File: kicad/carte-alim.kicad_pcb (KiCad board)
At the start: 2 copper layers, 96.5 x 45.7 mm, 52 parts, among them P1 BATT, P10 5V, P11 5V, P12 5V, P13 5V, P14 5V, P15 5V, P16 5V, P17 3.3V, P18 3.3V, P19 3.3V, P2 BATT, P20 3.3V, P21 3.3V, P22 3.3V, P23 3.3V, P24 3.3V, P25 3.3V, P26 3.3V, P27 MASSE, P28 MASSE, P29 PILES, P3 BATT, P30 CONN_1, P31 CONN_1, P32 CONN_1, P4 BATT, P5 BATT, P6 BATT, P7 5V, P8 5V, P9 5V, U1 LM_1117_3.3, U2 OKI_78SR_5

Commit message: Mise en qualité du typon
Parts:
- removed P1: BATT, KK_2C
- removed P21, P26: 3.3V, KK_2C
- added P33: CONN_1, Mounting_Holes:MountingHole_3.2mm_M3_Pad, F.Cu at (208.9, 66.7)
- C1, C2, C3, C4: footprint C2 -> Capacitors_THT:C_Rect_L7.0mm_W3.5mm_P2.50mm_P5.00mm
- C5, C6, C7, C8: footprint C2V10 -> Capacitors_THT:CP_Radial_D10.0mm_P2.50mm_P5.00mm
- D1, D2, D3, D4: footprint D4 -> Diodes_THT:D_DO-15_P10.16mm_Horizontal
- D5, D6, D7: footprint LED-3MM -> LEDs:LED_D3.0mm
- P10, P11, P12, P13, P14, P15, P16, P17, P18, P19, P2, P20, P22, P23, P24, P25, P29, P3, P4, P5, P6, P7, P8, P9: footprint KK_2C -> EPSA_Connect:KK_2C
- P27, P28: footprint SIL-8 -> Pin_Headers:Pin_Header_Straight_1x08_Pitch2.54mm
- P30, P31, P32: footprint 1pin -> Mounting_Holes:MountingHole_3.2mm_M3_Pad
- R1, R2, R3: footprint R3 -> Resistors_THT:R_Axial_DIN0207_L6.3mm_D2.5mm_P7.62mm_Horizontal
- U1: value LM_1117_3.3 -> LM 1117 3.3; footprint TO220_VERTICAL -> TO_SOT_Packages_THT:TO-220-3_Vertical
- U2: value OKI_78SR_5 -> OKI 78SR 5; footprint TO220_VERTICAL -> TO_SOT_Packages_THT:TO-220-3_Vertical
- moved P31 31.7 mm to (121.3, 103.5)
- moved P27 12.9 mm to (205.1, 94.6), turned to 180 degrees
- moved P28 12.7 mm to (209.6, 94.6), turned to 180 degrees
- moved P30 8.47 mm to (121.3, 66.7)
- moved P32 8.28 mm to (208.9, 103.5)
- moved P29 5.72 mm to (128.9, 102.9)
- moved D1 5.08 mm to (120.7, 83.8), turned to 270 degrees
- moved D2 5.08 mm to (128.3, 83.8), turned to 270 degrees
- moved D3 5.08 mm to (124.5, 94.0), turned to 90 degrees
- moved D4 5.08 mm to (132.1, 94.0), turned to 90 degrees
- moved R1 3.81 mm to (171.4, 96.5)
- moved R2 3.81 mm to (191.8, 96.5)
- moved R3 3.81 mm to (143.5, 92.7)
- moved U1 2.54 mm to (180.3, 78.7), turned to 270 degrees
- moved U2 2.54 mm to (148.6, 78.7), turned to 270 degrees
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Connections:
- net +3.3V renamed +3V3
- D1 pad 1: N-000009 -> +BATT
- D1 pad 2: +BATT -> Net-(D1-Pad2)
- D2 pad 1: N-000005 -> +BATT
- D2 pad 2: +BATT -> Net-(D2-Pad2)
- D3 pad 1: GND -> Net-(D1-Pad2)
- D3 pad 2: N-000009 -> GND
- D4 pad 1: GND -> Net-(D2-Pad2)
- D4 pad 2: N-000005 -> GND
- P29 pad 1: N-000009 -> Net-(D1-Pad2)
- P29 pad 2: N-000005 -> Net-(D2-Pad2)
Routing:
- net GND: track 0.00 -> 47.7 mm
- net +3V3: track 123.6 -> 104.5 mm
- net N-000005: track 14.3 -> 0.00 mm
- net Net-(D1-Pad2): track 0.00 -> 14.0 mm
- net Net-(D2-Pad2): track 0.00 -> 12.7 mm
- net N-000009: track 12.5 -> 0.00 mm
- net +5V: track 129.8 -> 132.9 mm
- net +BATT: track 151.6 -> 148.6 mm
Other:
- outline, holes or cut-outs redrawn
- net class GND added: clearance 0.254, trace_width 0.5, via_dia 1.6002, via_drill 0.8001
- board text added: "Carte alimentation ERACL 2018"
- board text removed: "Carte alimentation 2017-2018"

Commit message: Réalisation du typon avec connecteurs Mini-Fit
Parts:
- removed the C1 at (137.2, 87.6)
- removed the C5 at (139.7, 80.0)
- removed D4: 5A, Diodes_THT:D_DO-15_P10.16mm_Horizontal
- removed D5, D6, D7: GREEN, LEDs:LED_D3.0mm
- removed P10, P11, P12, P13, P14, P15, P16, P9: 5V, EPSA_Connect:KK_2C
- removed P17, P18, P19, P20, P22, P23, P24, P25: 3.3V, EPSA_Connect:KK_2C
- removed the P2 at (137.2, 102.9)
- removed P28: MASSE, Pin_Headers:Pin_Header_Straight_1x08_Pitch2.54mm
- removed P29: PILES, EPSA_Connect:KK_2C
- removed the P3 at (143.5, 102.9)
- removed the P5 at (137.2, 67.3)
- removed the P6 at (143.5, 67.3)
- added J1: PWR_OUT, Connectors_Molex:Molex_MiniFit-JR-5569-04A2_2x02x4.20mm_Angled, F.Cu at (159.4, 94.0)
- added J10: PWR_OUT, Connectors_Molex:Molex_MiniFit-JR-5569-04A2_2x02x4.20mm_Angled, F.Cu at (154.9, 76.2)
- added J2: PWR_OUT, Connectors_Molex:Molex_MiniFit-JR-5569-04A2_2x02x4.20mm_Angled, F.Cu at (169.5, 94.0)
- added J3: PWR_OUT, Connectors_Molex:Molex_MiniFit-JR-5569-04A2_2x02x4.20mm_Angled, F.Cu at (179.7, 94.0)
- added J4: PWR_OUT, Connectors_Molex:Molex_MiniFit-JR-5569-04A2_2x02x4.20mm_Angled, F.Cu at (189.9, 94.0)
- added J5: PWR_OUT, Connectors_Molex:Molex_MiniFit-JR-5569-04A2_2x02x4.20mm_Angled, F.Cu at (200.0, 94.0)
- added J6: PWR_OUT, Connectors_Molex:Molex_MiniFit-JR-5569-04A2_2x02x4.20mm_Angled, F.Cu at (195.6, 76.2)
- added J7: PWR_OUT, Connectors_Molex:Molex_MiniFit-JR-5569-04A2_2x02x4.20mm_Angled, F.Cu at (185.4, 76.2)
- added J8: PWR_OUT, Connectors_Molex:Molex_MiniFit-JR-5569-04A2_2x02x4.20mm_Angled, F.Cu at (175.3, 76.2)
- added J9: PWR_OUT, Connectors_Molex:Molex_MiniFit-JR-5569-04A2_2x02x4.20mm_Angled, F.Cu at (165.1, 76.2)
- D1: value 5A -> YELLOW; footprint Diodes_THT:D_DO-15_P10.16mm_Horizontal -> LEDs:LED_D3.0mm
- D2: value 5A -> RED; footprint Diodes_THT:D_DO-15_P10.16mm_Horizontal -> LEDs:LED_D3.0mm
- D3: value 5A -> ORANGE; footprint Diodes_THT:D_DO-15_P10.16mm_Horizontal -> LEDs:LED_D3.0mm
- P1: renamed from P33; value CONN_1 -> MECA
- P2: renamed from P30; value CONN_1 -> MECA
- P3: renamed from P31; value CONN_1 -> MECA
- P4: value BATT -> PILES; footprint EPSA_Connect:KK_2C -> Connectors_Molex:Molex_MiniFit-JR-5569-02A2_2x01x4.20mm_Angled
- P5: renamed from P32; value CONN_1 -> MECA
- P7: value 5V -> +5V; footprint EPSA_Connect:KK_2C -> Pin_Headers:Pin_Header_Straight_1x08_Pitch2.54mm
- P8: value 5V -> +3.3V; footprint EPSA_Connect:KK_2C -> Pin_Headers:Pin_Header_Straight_1x08_Pitch2.54mm
- U1, U2: footprint TO_SOT_Packages_THT:TO-220-3_Vertical -> Project:TO-220-3_Horizontal_Radiat
- moved R3 66.6 mm to (126.4, 83.8), turned to 90 degrees
- moved P7 64.8 mm to (210.2, 76.2)
- moved P8 54.6 mm to (205.1, 76.2)
- moved R2 54.3 mm to (118.1, 86.4), turned to 0 degrees
- moved C2 54.2 mm to (135.9, 91.4)
- moved U1 49.7 mm to (130.8, 82.5), turned to 0 degrees
- moved C1 49.0 mm to (139.1, 85.1), turned to 90 degrees
- moved C3 36.1 mm to (134.6, 99.1), turned to 270 degrees
- moved C4 33.5 mm to (142.2, 100.3), turned to 270 degrees
- moved P4 26.7 mm to (129.5, 94.0)
- moved R1 25.4 mm to (118.1, 94.0), turned to 0 degrees
- moved P6 18.6 mm to (207.6, 76.2), turned to 0 degrees
- moved C5 17.0 mm to (149.9, 104.1), turned to 90 degrees
- moved D1 14.2 mm to (123.2, 97.8), turned to 180 degrees
- moved C6 13.1 mm to (148.0, 90.2), turned to 270 degrees
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- renumbered C3 to C1, C7 to C2, C2 to C3, C6 to C4, C4 to C5, C8 to C6, P27 to P6, R3 to R1, R1 to R2, R2 to R3
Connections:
- D1 pad 1: +BATT -> GND
- D2 pad 1: +BATT -> GND
- D3 pad 1: Net-(D1-Pad2) -> GND
- D3 pad 2: GND -> Net-(D3-Pad2)
- P4 pad 1: +BATT -> GND
- P4 pad 2: GND -> +BATT
- P7 pad 2: GND -> +5V
- P8 pad 1: +5V -> +3V3
- P8 pad 2: GND -> +3V3
- R1 pad 1: Net-(D5-Pad1) -> Net-(D1-Pad2)
- R2 pad 1: Net-(D6-Pad1) -> Net-(D2-Pad2)
- R3 pad 1: Net-(D7-Pad1) -> Net-(D3-Pad2)
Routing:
- net +5V: track 132.9 -> 17.2 mm
- net +3V3: track 104.5 -> 20.9 mm
- net Net-(D1-Pad2): track 14.0 -> 4.86 mm
- net GND: track 47.7 -> 38.9 mm
- net Net-(D2-Pad2): track 12.7 -> 4.86 mm
- net Net-(D5-Pad1): track 5.61 -> 0.00 mm
- net Net-(D7-Pad1): track 3.81 -> 0.00 mm
- net Net-(D6-Pad1): track 3.81 -> 0.00 mm
- net Net-(D3-Pad2): track 0.00 -> 3.70 mm
- net +BATT: track 148.6 -> 146.8 mm
- added copper zone on In1.Cu, net +3V3
- added copper zone on In2.Cu, net +5V
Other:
- copper layers 2 -> 4
- net class Battery added: clearance 0.254, trace_width 1.5, via_dia 1.6002, via_drill 0.8001
- net class GND removed
- net class planes added: clearance 0.254, trace_width 0.5, via_dia 1.6002, via_drill 0.8001
- board text added: "+3.3V"
- board text added: "+5V"
- board text added: "+BATT"
- board text removed: "3.3V"
- board text removed: "5V"
- board text removed: "BATT"
- board text removed: "PILES"

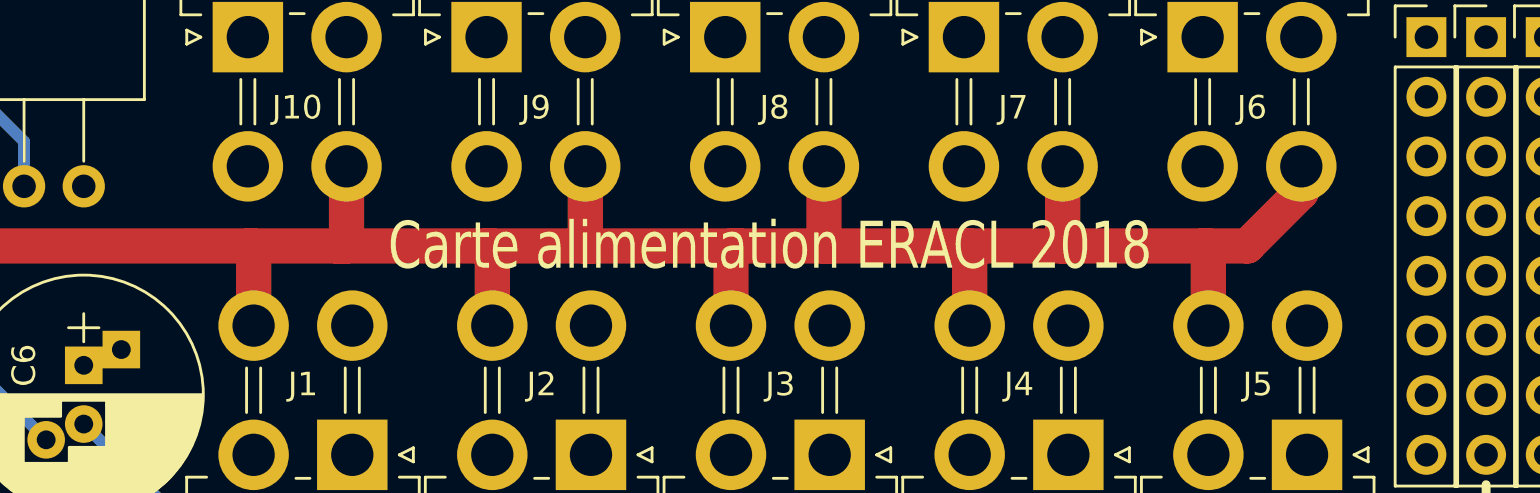
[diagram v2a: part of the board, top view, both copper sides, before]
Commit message: Mise à jour de la version dans les cartouches et la sérigraphie
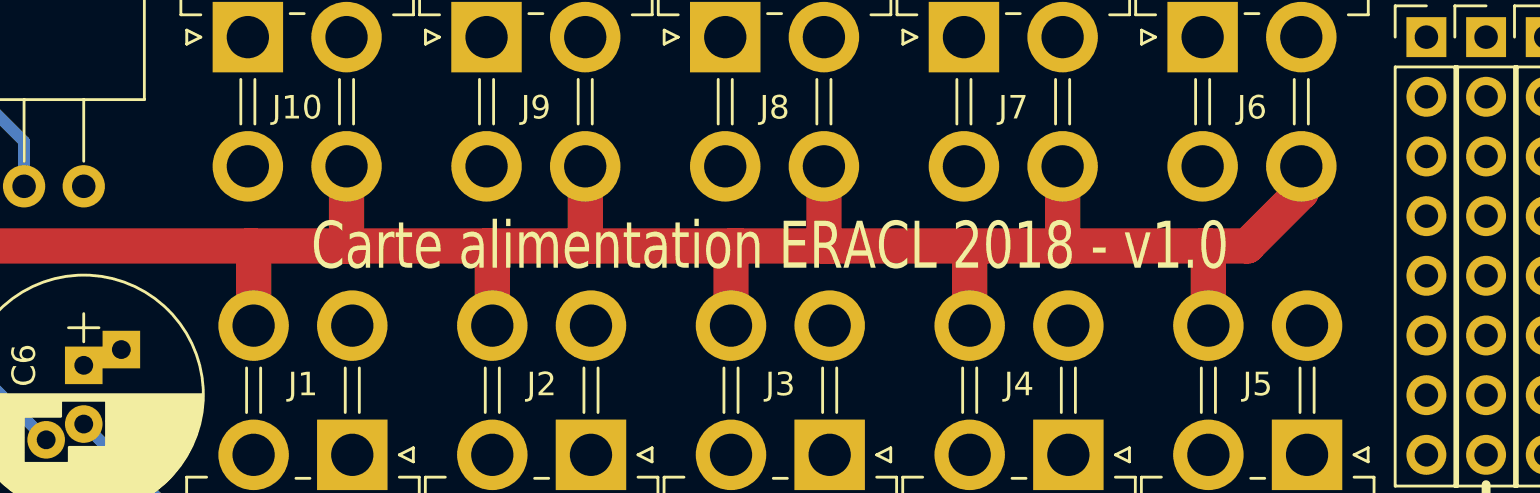
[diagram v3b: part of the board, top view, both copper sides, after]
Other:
- board text added: "Carte alimentation ERACL 2018 - v1.0"
- board text removed: "Carte alimentation ERACL 2018"
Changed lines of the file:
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@@
     (links 101)
     (no_connects 0)
-    (area 116.649499 62.039499 213.550501 108.140501)
+    (area 115.57 60.96 214.630001 109.220001)
     (thickness 1.6002)
     (drawings 17)
@@
   (title_block
     (title "Carte alimentation")
+    (date 2018-02-11)
+    (rev v1.0)
     (company "Centrale Lyon")
     (comment 1 "ERACL 2A 2018")
@@
   (gr_arc (start 121.285 66.675) (end 116.84 66.675) (angle 90) (layer Edge.Cuts) (width 0.381))
   (gr_arc (start 208.915 66.675) (end 208.915 62.23) (angle 90) (layer Edge.Cuts) (width 0.381))
-  (gr_text "Carte alimentation ERACL 2018" (at 177.165 85.09) (layer F.SilkS)
+  (gr_text "Carte alimentation ERACL 2018 - v1.0" (at 177.165 85.09) (layer F.SilkS)
     (effects (font (size 2 1.5) (thickness 0.2)))
   )
